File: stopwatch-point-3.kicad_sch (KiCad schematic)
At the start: 81 parts, among them J1 lipo, J4 USB_C_Receptacle_USB2.0_16P, J5 LS013B7DH03, Q1 AO3400A, Q2 2N7002, SW10 SW_Push, SW11 SW_Push_SPDT, SW5 BOOT, SW6 RESET, SW7 SW_Push, SW8 SW_Push, SW9 SW_Push, U1 USBLC6-2SC6, U2 TPS63001, U3 MAX17048, U4 BQ24075RGT, U8 STM32U073CBTx, Y1 ABS07-32.768KHZ-T

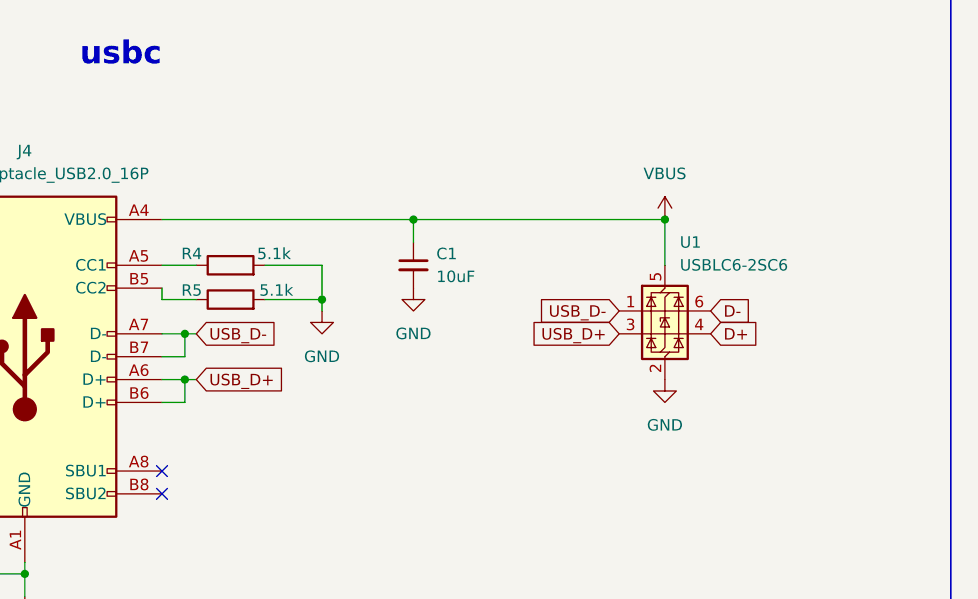
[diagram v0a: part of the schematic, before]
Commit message: add art + minor pcb changes
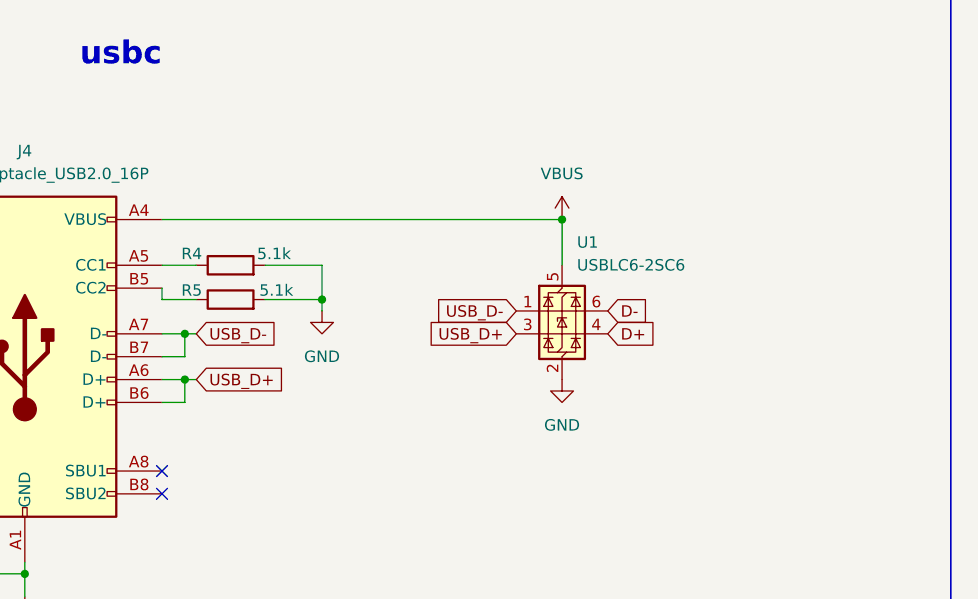
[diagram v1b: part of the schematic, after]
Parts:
- removed C1: 10uF, Capacitor_SMD:C_0402_1005Metric, symbol Device:C_Small
- TP2: footprint TestPoint:TestPoint_Pad_D2.0mm -> TestPoint:TestPoint_Pad_2.0x2.0mm
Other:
- moved on the sheet: U1

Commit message: minor edits
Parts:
- C10, C28: value 0.1uF -> 100nF; LCSC (none) -> C60474
- C11, C12, C23: LCSC (none) -> C29266
- C13: footprint Capacitor_SMD:C_0603_1608Metric -> Capacitor_SMD:C_0805_2012Metric; LCSC (none) -> C141660
- C17, C27, C29, C30: LCSC (none) -> C15525
- C18, C26: LCSC (none) -> C5137579
- C19, C20, C21, C22, C24, C25, C31: LCSC (none) -> C60474
- C3, C7, C8: LCSC (none) -> C368809
- D1: value LED -> green; LCSC (none) -> C74338
- D10, D11, D12, D2, D6, D8, D9: LCSC (none) -> C52917434
- D3: value LED -> orange; LCSC (none) -> C28310436
- L1: LCSC (none) -> C42455275
- Q1: LCSC (none) -> C347475
- Q2: LCSC (none) -> C8545
- R1, R10, R15, R3, R6, R7: LCSC (none) -> C106232
- R11, R8: LCSC (none) -> C2933074
- R12: LCSC (none) -> C2909346
- R13: value 100R -> 100; LCSC (none) -> C106232
- R14, R9: LCSC (none) -> C60490
- R16: LCSC (none) -> C2930002
- R17, R18: LCSC (none) -> C104375
- R2: LCSC (none) -> C106235
- SW10, SW7, SW8, SW9: LCSC (none) -> C110293
- SW11: LCSC (none) -> C2681570
- SW5, SW6: LCSC (none) -> C720477
- TP1, TP10, TP11, TP2, TP3, TP4, TP5, TP6, TP7, TP8, TP9: now not fitted
- U2: LCSC (none) -> C28060
- U3: LCSC (none) -> C2682616
- U4: LCSC (none) -> BQ24075RGTR
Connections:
- no-connect marks 5 -> 21
